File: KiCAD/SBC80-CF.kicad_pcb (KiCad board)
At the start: 2 copper layers, 100 x 75 mm, 18 parts, among them J1 Conn_02x20_Odd_Even, J2 I/O ADDR JP, J3 CF Card Conn, U1 74HC138, U2 74HC04

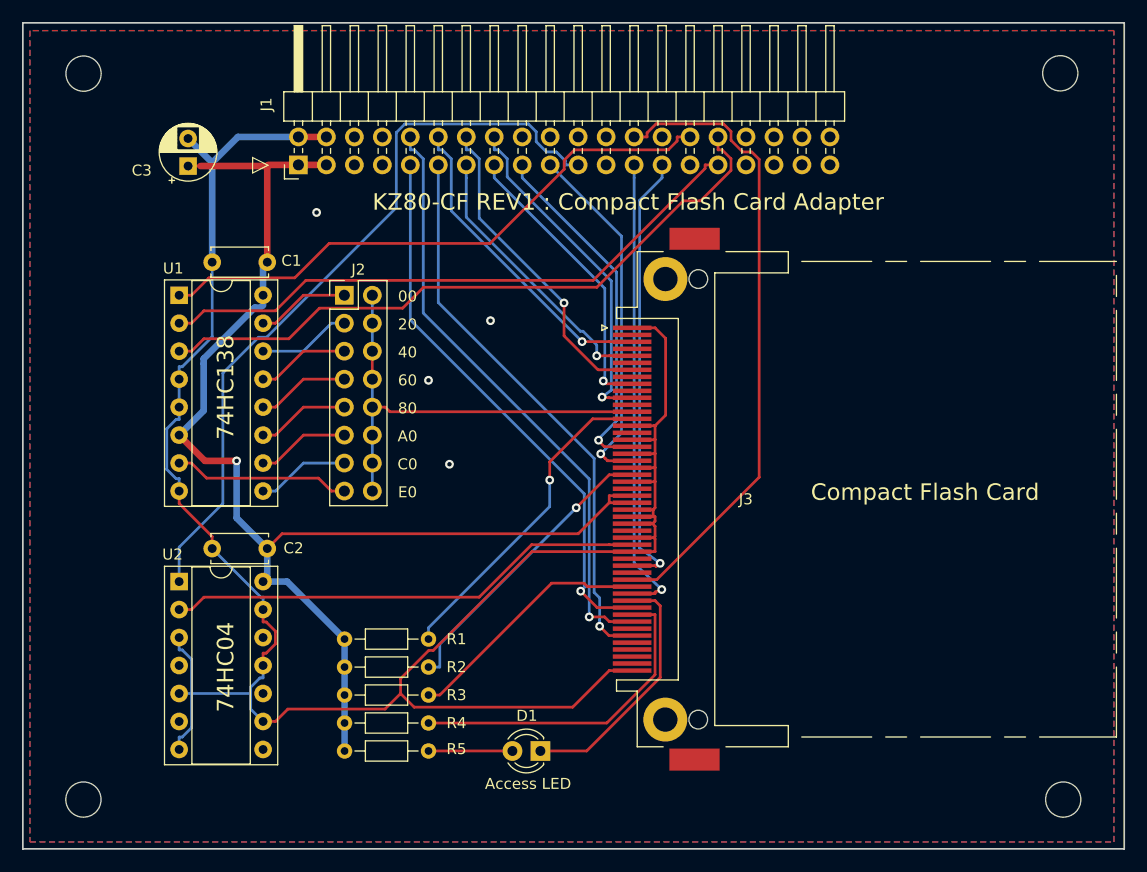
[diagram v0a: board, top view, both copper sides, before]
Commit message: CFカード部品変更 REV2基板整備
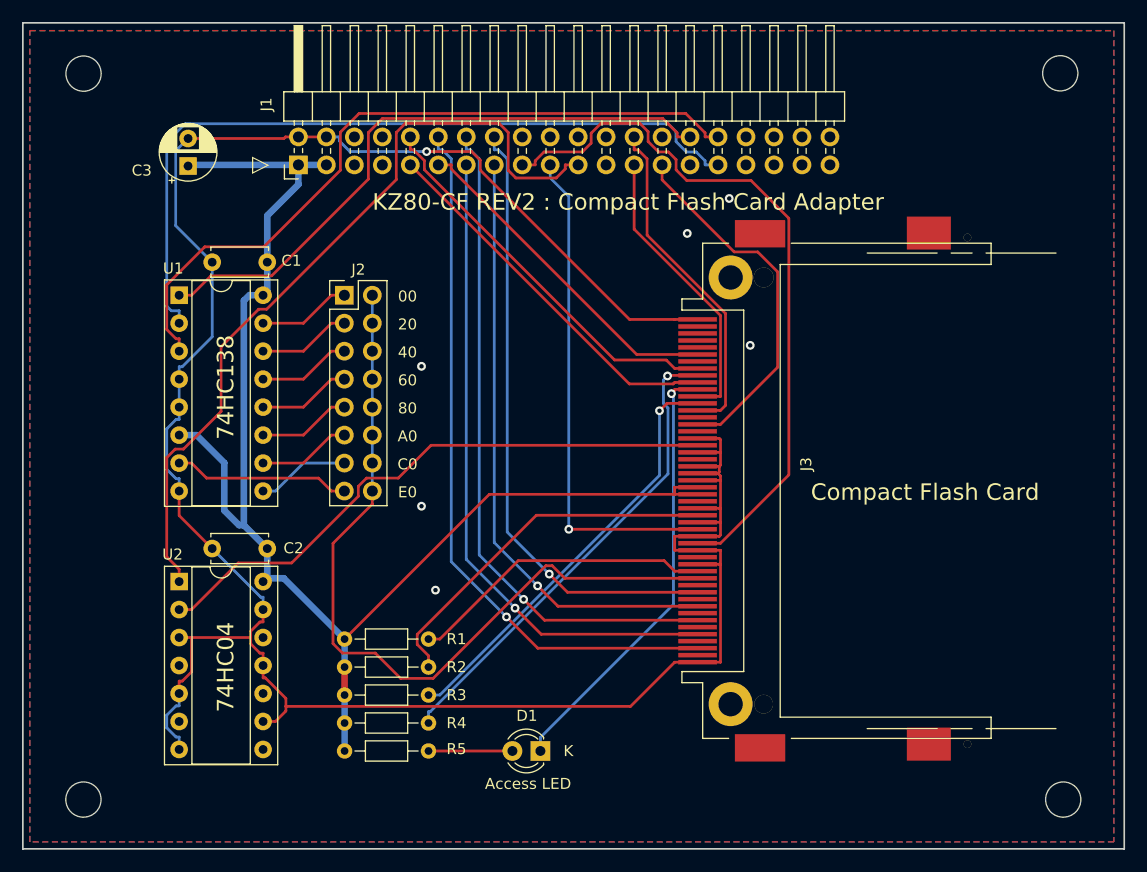
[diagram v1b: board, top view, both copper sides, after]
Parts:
- J3: footprint Connector_Card:CF-Card_Akituki -> Connector:CF-50P
- moved J3 5.89 mm to (163.3, 86.5), turned to 90 degrees
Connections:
- J1 pad 18: Net-(J1-Pad18) -> (no net)
- J1 pad 20: Net-(J1-Pad20) -> (no net)
- J1 pad 22: Net-(J1-Pad22) -> (no net)
- J1 pad 23: Net-(J1-Pad23) -> (no net)
- J1 pad 24: Net-(J1-Pad24) -> (no net)
- J1 pad 28: Net-(J1-Pad28) -> (no net)
- J1 pad 29: Net-(J1-Pad29) -> (no net)
- J1 pad 33: Net-(J1-Pad33) -> (no net)
- J1 pad 34: Net-(J1-Pad34) -> (no net)
- J1 pad 35: Net-(J1-Pad35) -> (no net)
- J1 pad 36: Net-(J1-Pad36) -> (no net)
- J1 pad 37: Net-(J1-Pad37) -> (no net)
- J1 pad 38: Net-(J1-Pad38) -> (no net)
- J1 pad 39: Net-(J1-Pad39) -> (no net)
- J1 pad 40: Net-(J1-Pad40) -> (no net)
- J1 pad 5: Net-(J1-Pad5) -> (no net)
- J1 pad 6: Net-(J1-Pad6) -> (no net)
- J1 pad 7: Net-(J1-Pad7) -> (no net)
- J1 pad 8: Net-(J1-Pad8) -> (no net)
- U2 pad 10: Net-(U2-Pad10) -> (no net)
- U2 pad 12: Net-(U2-Pad12) -> (no net)
- U2 pad 4: Net-(U2-Pad4) -> (no net)
- U2 pad 6: Net-(U2-Pad6) -> (no net)
- U2 pad 8: Net-(U2-Pad8) -> (no net)
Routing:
- net /D3: track 28.8 -> 64.9 mm
- net /D4: track 25.6 -> 59.6 mm
- net ~IORD: track 32.9 -> 65.3 mm, vias 1 -> 0
- net /D5: track 29.4 -> 60.9 mm
- net /~CS0: track 41.5 -> 72.2 mm
- net /D6: track 26.6 -> 55.1 mm
- net /A1: track 58.1 -> 30.8 mm
- net /D7: track 31.4 -> 56.1 mm
- net GND: track 198.9 -> 223.1 mm, vias 4 -> 7
- net /D2: track 51.3 -> 30.9 mm, vias 1 -> 0
- net /D1: track 54.6 -> 36.0 mm, vias 1 -> 0
- net /~DASP: track 22.9 -> 40.1 mm, vias 0 -> 1
- net /D0: track 50.7 -> 34.4 mm, vias 1 -> 0
- net /A0: track 42.5 -> 26.4 mm, vias 1 -> 0
- net /~DMACK: track 22.8 -> 38.8 mm, vias 0 -> 1
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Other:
- net class BOLD added: clearance 0.2, trace_width 0.6, via_dia 0.8, via_drill 0.4
- board text added: "K"
- board text added: "KZ80-CF REV2 : Compact Flash Card Adapter"
- board text removed: "KZ80-CF REV1 : Compact Flash Card Adapter"

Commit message: シルクパターン等整備
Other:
- board text added: "CF I/O ADDR"
- board text added: "Designed by tomi9"
- board text added: "Footprint"
- board text added: "KUNI-NET"
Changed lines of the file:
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@@
   (general
     (thickness 1.6)
-    (drawings 20)
+    (drawings 24)
     (tracks 380)
     (zones 0)
@@
     (pad "" smd rect (at -23.34 2.67 90) (size 2.49 4.57) (layers F.Cu F.Paste B.SilkS F.Mask))
   )
+  (gr_text KUNI-NET (at 135.83 63.12) (layer F.SilkS)
+    (effects (font (size 1.5 1.5) (thickness 0.3)))
+  )
+  (gr_text "CF I/O ADDR" (at 130.115 89.79) (layer F.SilkS)
+    (effects (font (size 1 1) (thickness 0.15)))
+  )
+  (gr_text "Designed by tomi9" (at 184.09 93.42) (layer F.SilkS)
+    (effects (font (size 1.5 1.5) (thickness 0.3)))
+  )
+  (gr_text Footprint (at 178.375 90.425) (layer F.SilkS)
+    (effects (font (size 1.5 1.5) (thickness 0.3)))
+  )
   (gr_text K (at 148.53 110.11) (layer F.SilkS)
     (effects (font (size 1 1) (thickness 0.2)))
@@
     (effects (font (size 1 1) (thickness 0.15)))
   )
-  (gr_text "KZ80-CF REV2 : Compact Flash Card Adapter" (at 153.96 60.27) (layer F.SilkS)
+  (gr_text "KZ80-CF REV2 : Compact Flash Card Adapter" (at 149.165 60.27) (layer F.SilkS)
     (effects (font (size 1.5 1.5) (thickness 0.3)))
   )
-  (gr_text "Compact Flash Card" (at 180.915 86.615) (layer F.SilkS)
+  (gr_text "Compact Flash Card" (at 184.725 80.265) (layer F.SilkS)
     (effects (font (size 1.5 1.5) (thickness 0.3)))
   )
